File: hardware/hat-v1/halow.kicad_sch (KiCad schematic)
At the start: 8 parts, among them J3 mPCIe 5.2H

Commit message: HAT v1 schematic: apply adversarial review (power + digital/security/DFM)
AUTO-ON above buck EN window, BENCH no longer blocks power-off, OVP moved
to 19.2 V with input damper, Tier A parts DNP for JLC, debug links
removable for production, antenna short limited, stock footprints where
available, cap ratings/DC-bias fixes, CONSOLE_TX/RX naming.

Co-Authored-By: Claude Opus 5.5 <noreply@anthropic.com>
Claude-Session: https://claude.ai/code/session_01MLRuxTEmuMV82xcNLE62jW
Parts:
- H5, H6: now left out of the parts list
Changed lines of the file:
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@@
   (global_label "GND" (shape passive) (at 40.64 107.95 0) (fields_autoplaced) (effects (font (size 1.27 1.27)) (justify left))
     (property "Intersheetrefs" "${INTERSHEET_REFS}" (at 40.64 107.95 0) (effects (font (size 1.27 1.27)) hide)))
-  (symbol (lib_id "batman:MH") (at 66.04 107.95 0) (unit 1) (in_bom yes) (on_board yes) (dnp no)
+  (symbol (lib_id "batman:MH") (at 66.04 107.95 0) (unit 1) (in_bom no) (on_board yes) (dnp no)
     (property "Reference" "H5" (at 66.04 105.41 0) (effects (font (size 1.27 1.27)) (justify bottom)))
     (property "Value" "M2 SMT standoff ~3.1mm" (at 66.04 110.49 0) (effects (font (size 1.27 1.27)) (justify top)))
@@
   (global_label "GND" (shape passive) (at 60.96 107.95 180) (fields_autoplaced) (effects (font (size 1.27 1.27)) (justify right))
     (property "Intersheetrefs" "${INTERSHEET_REFS}" (at 60.96 107.95 0) (effects (font (size 1.27 1.27)) hide)))
-  (symbol (lib_id "batman:MH") (at 96.52 107.95 0) (unit 1) (in_bom yes) (on_board yes) (dnp no)
+  (symbol (lib_id "batman:MH") (at 96.52 107.95 0) (unit 1) (in_bom no) (on_board yes) (dnp no)
     (property "Reference" "H6" (at 96.52 105.41 0) (effects (font (size 1.27 1.27)) (justify bottom)))
     (property "Value" "M2 SMT standoff ~3.1mm" (at 96.52 110.49 0) (effects (font (size 1.27 1.27)) (justify top)))

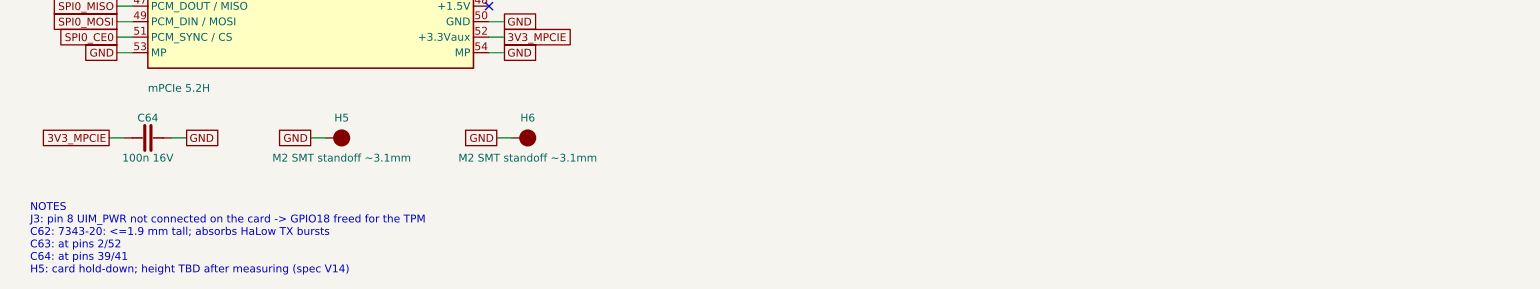
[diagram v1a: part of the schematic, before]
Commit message: HAT v1 layout v2: real Würth standoff in the escape proof; H6 corner fix; Freerouting G2 preview
- src_board.py: copy of the main board with footprints swapped to match design.py (H5/H6 ->
  Wurth WA-SMSI M2); export_fp.py / escape.py read SRC_BOARD and print the board they load.
- H5/H6 standoffs: Würth 9774030243R footprint (pad D5.3 + NPTH D3.0), design.py / gen_fp.py.
- G0 conflicts from the 5.8 courtyard fixed by a min-displacement search (C6/R9, U2/R6, C34);
  review fixes: EN_5V hand track follows C34, J1 not moved (J1 x H5 courtyard_exempt, sketch.py
  supports it), no-via ring r3.05 and NPTH keep-out r1.8 around H5/H6 in escape.py.
- Full escape: power 31/31 routed, VSYS necks 1.90 / 1.19 mm, 0 vias within r3.05 of H5/H6,
  remaining signals 45/65 (escape-full.log).
- frpreview.py + frprev/run2.sh: Freerouting on the escape board with only the planned power
  copper kept. Two runs: 102 / 95 unconnected (DRC), concentrated outside the power zones
  (card underside Z5/Z6, J3 side, GNSS, top strip). G1 on hold (PLAN §13).
- PLAN §12 (+3 mm left, power re-place) kept as a reviewed backup plan; HANDOFF §9.

Co-Authored-By: Claude Opus 5.5 <noreply@anthropic.com>
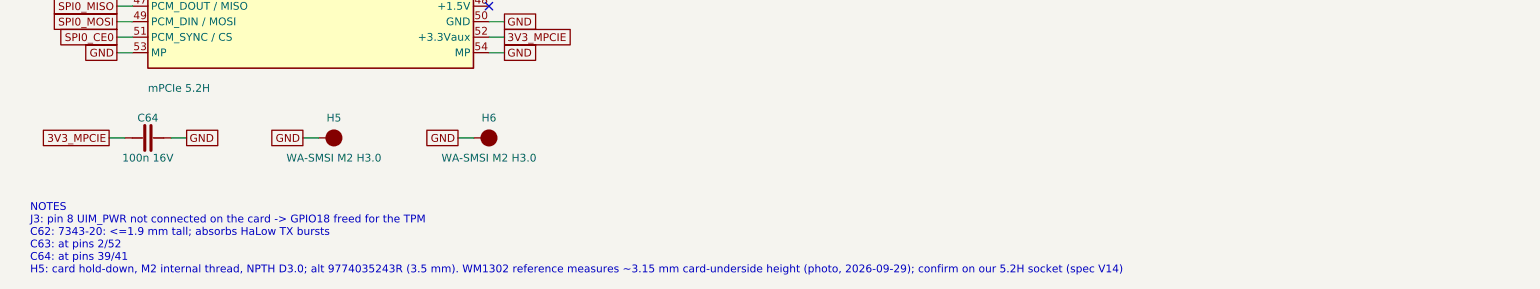
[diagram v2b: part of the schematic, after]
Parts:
- H5: value M2 SMT standoff ~3.1mm -> WA-SMSI M2 H3.0; footprint batman:SMT_Standoff_M2_TBD -> batman:Wurth_WA-SMSI_M2_OD4.35; MPN (none) -> 9774030243R; Manufacturer (none) -> Wurth Elektronik; Note card hold-down; height TBD after measuring (spec V14) -> card hold-down, M2 internal thread, NPTH D3.0; alt 97740352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; now in the parts list
- H6: value M2 SMT standoff ~3.1mm -> WA-SMSI M2 H3.0; footprint batman:SMT_Standoff_M2_TBD -> batman:Wurth_WA-SMSI_M2_OD4.35; MPN (none) -> 9774030243R; Manufacturer (none) -> Wurth Elektronik; now in the parts list
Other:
- note added: "NOTES J3: pin 8 UIM_PWR not connected on the card -> GPIO18 freed for the TPM C62: 7343-20: <=1.9 mm tall; absorbs HaLow TX bursts C63: at pins 2/52 C64: at pins 39/41 H5: card hold-down, M2 internal thread, NPTH D3.0; alt 9774035243R (3.5 mm). WM1302 reference measures ~3.15 mm card-underside height (photo, 2026-09-29); confirm on our 5.2H socket (spec V14)"
- note removed: "NOTES J3: pin 8 UIM_PWR not connected on the card -> GPIO18 freed for the TPM C62: 7343-20: <=1.9 mm tall; absorbs HaLow TX bursts C63: at pins 2/52 C64: at pins 39/41 H5: card hold-down; height TBD after measuring (spec V14)"
- moved on the sheet: H5, H6
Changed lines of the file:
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@@
   (global_label "GND" (shape passive) (at 40.64 107.95 0) (fields_autoplaced) (effects (font (size 1.27 1.27)) (justify left))
     (property "Intersheetrefs" "${INTERSHEET_REFS}" (at 40.64 107.95 0) (effects (font (size 1.27 1.27)) hide)))
-  (symbol (lib_id "batman:MH") (at 66.04 107.95 0) (unit 1) (in_bom no) (on_board yes) (dnp no)
-    (property "Reference" "H5" (at 66.04 105.41 0) (effects (font (size 1.27 1.27)) (justify bottom)))
-    (property "Value" "M2 SMT standoff ~3.1mm" (at 66.04 110.49 0) (effects (font (size 1.27 1.27)) (justify top)))
-    (property "Footprint" "batman:SMT_Standoff_M2_TBD" (at 66.04 107.95 0) (effects (font (size 1.27 1.27)) hide))
-    (property "Datasheet" "" (at 66.04 107.95 0) (effects (font (size 1.27 1.27)) hide))
-    (property "MPN" "" (at 66.04 107.95 0) (effects (font (size 1.27 1.27)) hide))
-    (property "Manufacturer" "" (at 66.04 107.95 0) (effects (font (size 1.27 1.27)) hide))
-    (property "Tier" "C" (at 66.04 107.95 0) (effects (font (size 1.27 1.27)) hide))
-    (property "LCSC" "" (at 66.04 107.95 0) (effects (font (size 1.27 1.27)) hide))
-    (property "Note" "card hold-down; height TBD after measuring (spec V14)" (at 66.04 107.95 0) (effects (font (size 1.27 1.27)) hide))
+  (symbol (lib_id "batman:MH") (at 64.77 107.95 0) (unit 1) (in_bom yes) (on_board yes) (dnp no)
+    (property "Reference" "H5" (at 64.77 105.41 0) (effects (font (size 1.27 1.27)) (justify bottom)))
+    (property "Value" "WA-SMSI M2 H3.0" (at 64.77 110.49 0) (effects (font (size 1.27 1.27)) (justify top)))
+    (property "Footprint" "batman:Wurth_WA-SMSI_M2_OD4.35" (at 64.77 107.95 0) (effects (font (size 1.27 1.27)) hide))
+    (property "Datasheet" "" (at 64.77 107.95 0) (effects (font (size 1.27 1.27)) hide))
+    (property "MPN" "9774030243R" (at 64.77 107.95 0) (effects (font (size 1.27 1.27)) hide))
+    (property "Manufacturer" "Wurth Elektronik" (at 64.77 107.95 0) (effects (font (size 1.27 1.27)) hide))
+    (property "Tier" "C" (at 64.77 107.95 0) (effects (font (size 1.27 1.27)) hide))
+    (property "LCSC" "" (at 64.77 107.95 0) (effects (font (size 1.27 1.27)) hide))
+    (property "Note" "card hold-down, M2 internal thread, NPTH D3.0; alt 9774035243R (3.5 mm). WM1302 reference measures ~3.15 mm card-underside height (photo, 2026-09-29); confirm on our 5.2H socket (spec V14)" (at 64.77 107.95 0) (effects (font (size 1.27 1.27)) hide))
     (pin "1")
     (instances (project "batman-hat" (path "/bad0bf22-4662-5834-886f-55d01014b15a/84737a6c-f701-542d-9454-519ca41a00ff" (reference "H5") (unit 1))))
   )
-  (wire (pts (xy 63.5 107.95) (xy 60.96 107.95)) (stroke (width 0) (type default)))
-  (global_label "GND" (shape passive) (at 60.96 107.95 180) (fields_autoplaced) (effects (font (size 1.27 1.27)) (justify right))
-    (property "Intersheetrefs" "${INTERSHEET_REFS}" (at 60.96 107.95 0) (effects (font (size 1.27 1.27)) hide)))
-  (symbol (lib_id "batman:MH") (at 96.52 107.95 0) (unit 1) (in_bom no) (on_board yes) (dnp no)
-    (property "Reference" "H6" (at 96.52 105.41 0) (effects (font (size 1.27 1.27)) (justify bottom)))
-    (property "Value" "M2 SMT standoff ~3.1mm" (at 96.52 110.49 0) (effects (font (size 1.27 1.27)) (justify top)))
-    (property "Footprint" "batman:SMT_Standoff_M2_TBD" (at 96.52 107.95 0) (effects (font (size 1.27 1.27)) hide))
-    (property "Datasheet" "" (at 96.52 107.95 0) (effects (font (size 1.27 1.27)) hide))
-    (property "MPN" "" (at 96.52 107.95 0) (effects (font (size 1.27 1.27)) hide))
-    (property "Manufacturer" "" (at 96.52 107.95 0) (effects (font (size 1.27 1.27)) hide))
-    (property "Tier" "C" (at 96.52 107.95 0) (effects (font (size 1.27 1.27)) hide))
-    (property "LCSC" "" (at 96.52 107.95 0) (effects (font (size 1.27 1.27)) hide))
-    (property "Note" "" (at 96.52 107.95 0) (effects (font (size 1.27 1.27)) hide))
+  (wire (pts (xy 62.23 107.95) (xy 59.69 107.95)) (stroke (width 0) (type default)))
+  (global_label "GND" (shape passive) (at 59.69 107.95 180) (fields_autoplaced) (effects (font (size 1.27 1.27)) (justify right))
+    (property "Intersheetrefs" "${INTERSHEET_REFS}" (at 59.69 107.95 0) (effects (font (size 1.27 1.27)) hide)))
+  (symbol (lib_id "batman:MH") (at 90.17 107.95 0) (unit 1) (in_bom yes) (on_board yes) (dnp no)
+    (property "Reference" "H6" (at 90.17 105.41 0) (effects (font (size 1.27 1.27)) (justify bottom)))
+    (property "Value" "WA-SMSI M2 H3.0" (at 90.17 110.49 0) (effects (font (size 1.27 1.27)) (justify top)))
+    (property "Footprint" "batman:Wurth_WA-SMSI_M2_OD4.35" (at 90.17 107.95 0) (effects (font (size 1.27 1.27)) hide))
+    (property "Datasheet" "" (at 90.17 107.95 0) (effects (font (size 1.27 1.27)) hide))
+    (property "MPN" "9774030243R" (at 90.17 107.95 0) (effects (font (size 1.27 1.27)) hide))
+    (property "Manufacturer" "Wurth Elektronik" (at 90.17 107.95 0) (effects (font (size 1.27 1.27)) hide))
+    (property "Tier" "C" (at 90.17 107.95 0) (effects (font (size 1.27 1.27)) hide))
+    (property "LCSC" "" (at 90.17 107.95 0) (effects (font (size 1.27 1.27)) hide))
+    (property "Note" "" (at 90.17 107.95 0) (effects (font (size 1.27 1.27)) hide))
     (pin "1")
     (instances (project "batman-hat" (path "/bad0bf22-4662-5834-886f-55d01014b15a/84737a6c-f701-542d-9454-519ca41a00ff" (reference "H6") (unit 1))))
   )
-  (wire (pts (xy 93.98 107.95) (xy 91.44 107.95)) (stroke (width 0) (type default)))
-  (global_label "GND" (shape passive) (at 91.44 107.95 180) (fields_autoplaced) (effects (font (size 1.27 1.27)) (justify right))
-    (property "Intersheetrefs" "${INTERSHEET_REFS}" (at 91.44 107.95 0) (effects (font (size 1.27 1.27)) hide)))
-  (text "NOTES\nJ3: pin 8 UIM_PWR not connected on the card -> GPIO18 freed for the TPM\nC62: 7343-20: <=1.9 mm tall; absorbs HaLow TX bursts\nC63: at pins 2/52\nC64: at pins 39/41\nH5: card hold-down; height TBD after measuring (spec V14)" (at 15 118.66 0) (effects (font (size 1.27 1.27)) (justify left top)))
+  (wire (pts (xy 87.63 107.95) (xy 85.09 107.95)) (stroke (width 0) (type default)))
+  (global_label "GND" (shape passive) (at 85.09 107.95 180) (fields_autoplaced) (effects (font (size 1.27 1.27)) (justify right))
+    (property "Intersheetrefs" "${INTERSHEET_REFS}" (at 85.09 107.95 0) (effects (font (size 1.27 1.27)) hide)))
+  (text "NOTES\nJ3: pin 8 UIM_PWR not connected on the card -> GPIO18 freed for the TPM\nC62: 7343-20: <=1.9 mm tall; absorbs HaLow TX bursts\nC63: at pins 2/52\nC64: at pins 39/41\nH5: card hold-down, M2 internal thread, NPTH D3.0; alt 9774035243R (3.5 mm). WM1302 reference measures ~3.15 mm card-underside height (photo, 2026-09-29); confirm on our 5.2H socket (spec V14)" (at 15 118.66 0) (effects (font (size 1.27 1.27)) (justify left top)))
 )
